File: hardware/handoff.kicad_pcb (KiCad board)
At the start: 2 copper layers, 40 x 62 mm, 52 parts, among them J1 BAT XH-2, J2 PAD JST-XH 2p, J3 LED JST-XH 4p / 5mm RGB, J5 CHG XH-2, SW1 SS-12F23G5, SW2 TACT 6x6, U1 Raspberry Pi Pico 2 W, U2 MCP6292-E/MS

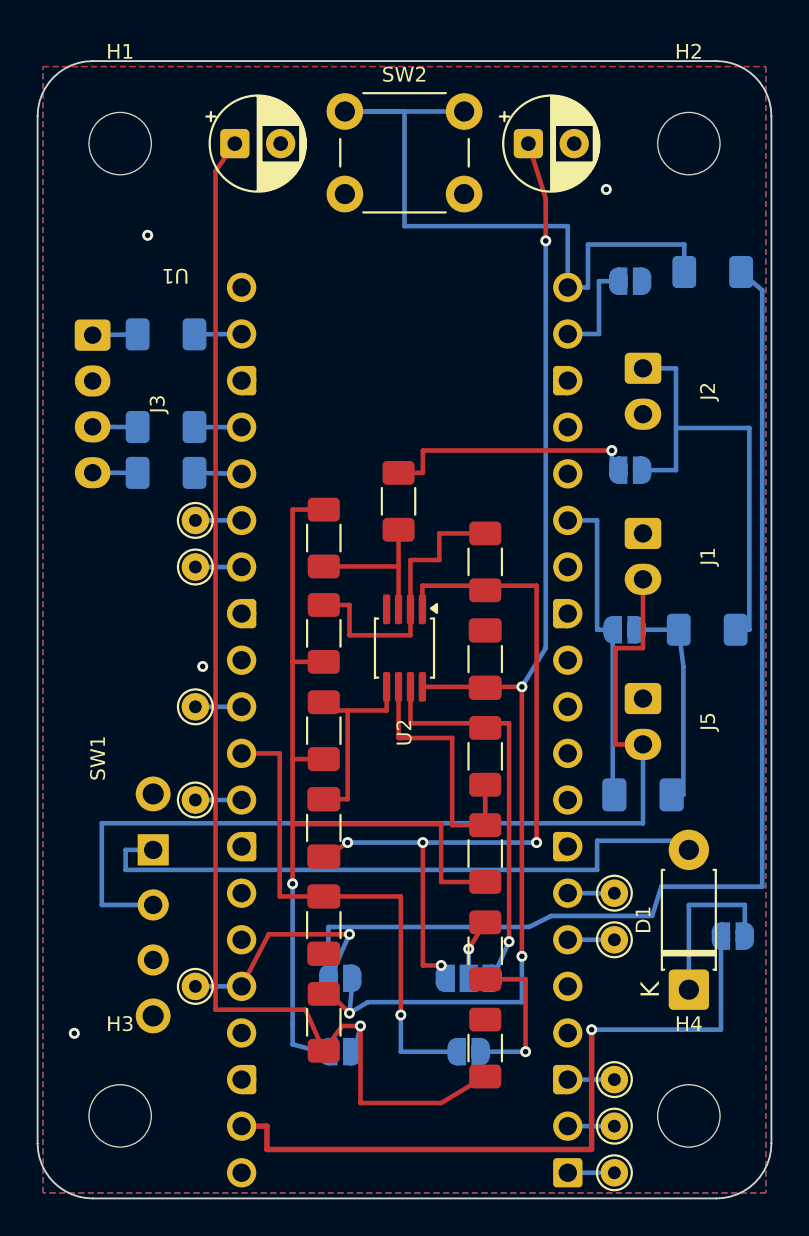
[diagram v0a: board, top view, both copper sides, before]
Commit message: Fix J3's overhang, the battery path, right-angle corners, edge clearance
Four things from the layout brief's known-wrong list, fixed together
because the battery path fix moved everything else on the thumb and
little-finger walls:

- J3 no longer overhangs the thumb edge (pin 1 moved from x 3.0 to
  x 4.0, flush with the housing's own courtyard).
- BAT+, SW_OUT, D1_K and VSYS moved from the little-finger wall to the
  thumb wall, where SW1 and J3 already are: one crossing of the board
  instead of three, and two pin-row threads instead of six. The
  SW_OUT U-turn and the JP4 redundant loop went with the routing they
  were part of.
- Every track corner is 45 degrees or straight. mitre() chamfers every
  right-angle join in a ROUTES polyline before it becomes copper, and
  two DRC rules (track_angle, track_segment_length) fail the run if a
  right angle or a stub comes back.
- +3V3 came off the little-finger wall (0.375 mm from the edge at
  0.25 mm, less once Power tracks are actually 0.5 mm): it now
  crosses the board once, at the elbow, into R15.

The VREF divider (R10, R11, JP6) moved to the hand end with its own
hold-up cap C4, off the elbow block, which frees the top lane on the
thumb side that VSYS now needs and removes a via.

Every footprint and text is now checked against the outline
programmatically (report()), not by eye: nothing may sit within
0.5 mm of the edge unless it is in OVERHANG (SW1's handle, U1's USB
courtyard). An independent short check (shorts(), SHAPE.Collide over
every pad/track/via/pour pair on each face) finds nothing under
0.2 mm. Board corners are fixed to 90-degree arcs (SetArcGeometry
with the midpoint on the corner; SetCenter/Start/End had been going
the long way round).

DRC: 0 error(s), 10 warning(s) (the ten deliberate
lib_footprint_mismatch); parity 0; unrouted 0 item(s).

Co-Authored-By: Claude Sonnet 5 <noreply@anthropic.com>
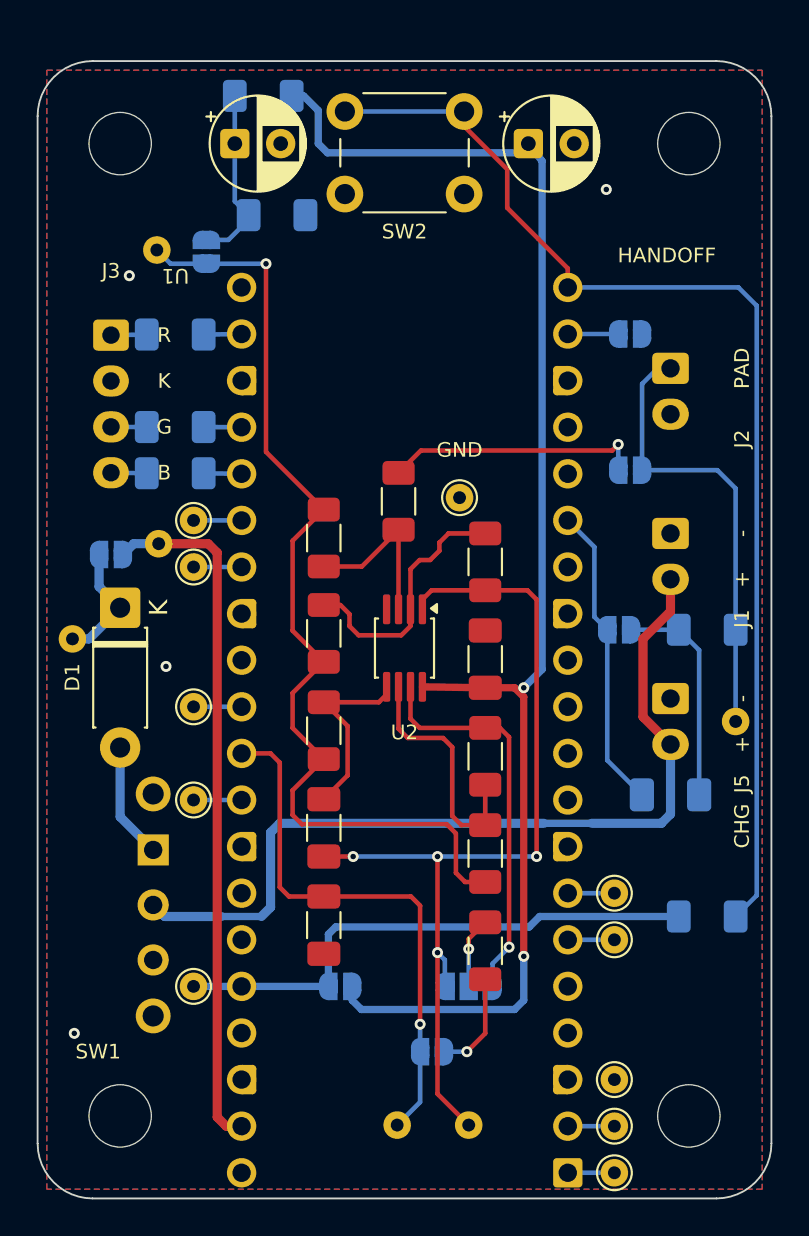
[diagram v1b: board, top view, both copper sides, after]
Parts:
- added TP1: GND, TestPoint:TestPoint_THTPad_D1.5mm_Drill0.7mm, F.Cu at (23.0, 23.8)
- added TP2: ADC0, TestPoint:TestPoint_THTPad_D1.5mm_Drill0.7mm, B.Cu at (19.6, 58.0)
- added TP3: OUT1, TestPoint:TestPoint_THTPad_D1.5mm_Drill0.7mm, B.Cu at (23.5, 58.0)
- added TP4: VREF, TestPoint:TestPoint_THTPad_D1.5mm_Drill0.7mm, B.Cu at (6.50, 10.3)
- added TP5: PAD, TestPoint:TestPoint_THTPad_D1.5mm_Drill0.7mm, B.Cu at (38.0, 36.0)
- added TP6: VSYS, TestPoint:TestPoint_THTPad_D1.5mm_Drill0.7mm, B.Cu at (6.60, 26.3)
- added TP7: D1_K, TestPoint:TestPoint_THTPad_D1.5mm_Drill0.7mm, B.Cu at (1.90, 31.5)
- R10, R11: moved to B.Cu
- moved R10 50.6 mm to (12.3, 1.90), turned to 180 degrees
- moved R11 46.8 mm to (13.1, 8.40), turned to 0 degrees
- moved JP6 44.2 mm to (9.20, 10.4), turned to -90 degrees
- moved JP5 39.8 mm to (4.00, 26.9), turned to 0 degrees
- moved D1 37.3 mm to (4.50, 29.8), turned to -90 degrees
- moved R15 35.1 mm to (36.5, 46.6), turned to 0 degrees
- moved JP8 2.88 mm to (32.3, 14.9)
- moved JP1 2.00 mm to (21.5, 54.0)
- moved C6 1.50 mm to (34.5, 40.0)
- moved J1 1.50 mm to (34.5, 25.8)
- moved J2 1.50 mm to (34.5, 16.8)
- moved J5 1.50 mm to (34.5, 34.8)
- moved J3 1.00 mm to (4.00, 14.9)
- moved R14 0.50 mm to (7.50, 22.5)
- moved R12 0.50 mm to (7.50, 14.9)
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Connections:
- net Net-(D1-K) renamed /D1_K
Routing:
- net Net-(JP6-A): track 69.9 -> 9.82 mm, vias 1 -> 0
- net +3V3: track 74.0 -> 29.7 mm, vias 1 -> 0
- net /SW_OUT: track 35.4 -> 6.33 mm
- net /BTN: track 38.4 -> 62.9 mm
- net /AFE_3V3: track 65.3 -> 78.6 mm, vias 4 -> 2
- net /OUT1: track 41.3 -> 50.1 mm
- net /BAT+: track 53.0 -> 47.2 mm
- net VREF: track 49.5 -> 54.4 mm
- net Net-(JP1-A): track 8.60 -> 5.61 mm
- net /ROLE: track 5.63 -> 2.75 mm
- net /ADC0: track 27.1 -> 29.6 mm
- net /D1_K: track 9.07 -> 6.68 mm
- net GND: track 2.30 -> 0.00 mm
- net Net-(U2A--): track 16.0 -> 14.2 mm
- net VSYS: track 39.0 -> 37.9 mm, vias 1 -> 0
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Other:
- board text added: "+"
- board text added: "-"
- board text added: "ADC0"
- board text added: "B"
- board text added: "CHG"
- board text added: "D1K"
- board text added: "G"
- board text added: "GND"
- board text added: "HANDOFF"
- board text added: "HANDOFF rev A - 2 layer, 40 x 62 mm, 1.6 mm FR-4, 1 oz Cu, HASL lead-free, green mask, white silk. Min track/space 0.25/0.2 (design), 0.15 (fab floor). Min drill 0.3 (vias), 0.7 (test pads). H1-H4 3.4 mm unplated."
- board text added: "HANDOFF rev A 2026-09"
- board text added: "JP1-8: OPEN = ISOLATED"
- board text added: "K"
- board text added: "OUT1"
- board text added: "PAD"
- board text added: "R"
- board text added: "VREF"
- board text added: "VSYS"

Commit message: Add the haptic motor, move the passives to 0603/0805, unstick the breakout pads
Three changes to the parts order, and one bug they surfaced.

The motor. A 10 mm coin motor (M1, off-board on leads into J6) switched
low-side by an AO3400A (Q1) from GP28, with a 100 R gate series (R16), a
100 k gate pull-down (R17, so the gate cannot float through BOOTSEL) and a
SOD-123 Schottky (D3) across the motor. It runs from VSYS, not the Pico's
3V3: 100 mA of pulsed motor current has no business on the rail that feeds
AFE_3V3 through JP4. The block sits on the bottom face at the thumb end of
the elbow, two millimetres from VSYS at pin 39 and a pour away from the AFE.
D3 has no SKU yet - it is the one part here not already on order.

The passives. 100 k, 10 k and the LED series resistors (now 100 R, not
330 R) are 0603; C4 and C5 are 0805 MLCC instead of 5 mm radial
electrolytics. 1 M, 1k5 and the C0G/X7R capacitors stay 1206 - they were not
re-ordered. Every 0603 pad moved 0.64 mm inward, which walked twenty-odd
track ends off their pads, so ROUTES now names pads - P("R6", "1") - and
gen_pcb.py resolves them against the placed footprint. The shift also closed
the 0.25 mm pour channel under R5 that is the AFE pour's only way out to the
electrode; R5 moved back 0.64 mm and VREF leaves its pad along the pad row
now. C4 and C5 changed face: their feeds were always on the bottom and
reached them through the electrolytics' leads.

The bug. E3, E4 and E10 broke out Pico pins 1, 2 and 3 at x 31.44, which put
their pads 3.3 mm from H4's centre - inside the 8 mm enclosure boss. DRC
missed it because the boss keep-out allows pads (the hole's own NPTH pad is
in the middle of it) and because the "bare pads have no body" rule excused
the courtyard overlap from either side. Both are fixed: report() checks every
pad against every boss circle, and the courtyard exemption no longer applies
against a mounting hole. Regression-tested. The breakouts are now GP3 (5),
GP22 (29) and GND (8); GP0 and GP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
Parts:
- added D3: 1N5819W, Diode_SMD:D_SOD-123, F.Cu at (16.9, 58.6)
- added J6: MOT 1x02 2.54, Connector_PinHeader_2.54mm:PinHeader_1x02_P2.54mm_Vertical, B.Cu at (14.9, 53.7)
- added Q1: AO3400A, Package_TO_SOT_SMD:SOT-23, B.Cu at (15.0, 60.0)
- added R16: 100, Resistor_SMD:R_0603_1608Metric_Pad0.98x0.95mm_HandSolder, F.Cu at (13.6, 47.9)
- added R17: 100k, Resistor_SMD:R_0603_1608Metric_Pad0.98x0.95mm_HandSolder, F.Cu at (14.5, 51.3)
- added TP8: AFE_3V3, TestPoint:TestPoint_THTPad_D1.5mm_Drill0.7mm, B.Cu at (27.5, 8.20)
- C4, C5: value 10uF 63V -> 10uF 100V; footprint Capacitor_THT:CP_Radial_D5.0mm_P2.50mm -> Capacitor_SMD:C_0805_2012Metric_Pad1.18x1.45mm_HandSolder; moved to B.Cu
- E10: value GND (pin 3) -> GND (pin 8)
- E3: value GP0 (pin 1) -> GP3 (pin 5)
- E4: value GP1 (pin 2) -> GP22 (pin 29)
- R10, R11, R15, R4, R5, R6, R7, R8: footprint Resistor_SMD:R_1206_3216Metric_Pad1.30x1.75mm_HandSolder -> Resistor_SMD:R_0603_1608Metric_Pad0.98x0.95mm_HandSolder
- R12, R13, R14: value 330 -> 100; footprint Resistor_SMD:R_1206_3216Metric_Pad1.30x1.75mm_HandSolder -> Resistor_SMD:R_0603_1608Metric_Pad0.98x0.95mm_HandSolder
- moved E4 34.2 mm to (8.50, 32.7)
- moved E10 12.7 mm to (31.4, 42.8)
- moved E3 10.2 mm to (31.4, 50.4)
- moved C4 1.25 mm to (11.8, 5.20)
- moved C5 1.04 mm to (27.8, 4.50)
- moved R10 0.64 mm to (11.7, 1.90)
- moved R11 0.64 mm to (12.4, 8.40)
- moved R5 0.64 mm to (15.6, 30.6)
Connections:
- E3 pad 1: /GP0 -> /GP3
- E4 pad 1: /GP1 -> /GP22
- U1 pad 1: /GP0 -> unconnected-(U1-GPIO0-Pad1)
- U1 pad 2: /GP1 -> unconnected-(U1-GPIO1-Pad2)
- U1 pad 29: unconnected-(U1-GPIO22-Pad29) -> /GP22
- U1 pad 34: unconnected-(U1-GPIO28_ADC2-Pad34) -> /MOT_DRV
- U1 pad 5: unconnected-(U1-GPIO3-Pad5) -> /GP3
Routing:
- net Net-(Q1-G): track 0.00 -> 13.5 mm, vias 0 -> 1
- net /MOT_SW: track 0.00 -> 10.2 mm, vias 0 -> 1
- net VSYS: track 37.9 -> 44.8 mm
- net /MOT_DRV: track 0.00 -> 3.37 mm
- net /GP22: track 0.00 -> 2.62 mm
- net /GP3: track 0.00 -> 2.30 mm
- net /GP1: track 2.30 -> 0.00 mm
- net /GP0: track 2.30 -> 0.00 mm
- net GND: track 0.00 -> 2.12 mm, vias 4 -> 5
- net Net-(U2B--): track 13.6 -> 12.0 mm
- net /AFE_3V3: track 78.6 -> 79.9 mm
- net /OUT1: track 50.1 -> 51.4 mm
- net +3V3: track 29.7 -> 30.3 mm
- net /LED_G: track 2.07 -> 2.71 mm
- net /J3_G: track 1.95 -> 2.59 mm
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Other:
- board text added: "HANDOFF rev A - 2 layer, 40 x 62 mm, 1.6 mm FR-4, 1 oz Cu, HASL lead-free, green mask, white silk. Min track/space 0.25/0.2 (design), 0.15 (fab floor). Min solder-mask dam 0.1. Drills 0.3 / 0.7 / 0.95 / 1.0 / 1.1 / 1.15 PTH and 3.4 NPTH - see build/drills.md. H1-H4 3.4 mm unplated, each inside an 8 mm enclosure boss."
- board text added: "JP1-8 = OPEN"
- board text added: "MOT"
- board text removed: "HANDOFF rev A - 2 layer, 40 x 62 mm, 1.6 mm FR-4, 1 oz Cu, HASL lead-free, green mask, white silk. Min track/space 0.25/0.2 (design), 0.15 (fab floor). Min drill 0.3 (vias), 0.7 (test pads). H1-H4 3.4 mm unplated."
- board text removed: "JP1-8: OPEN = ISOLATED"

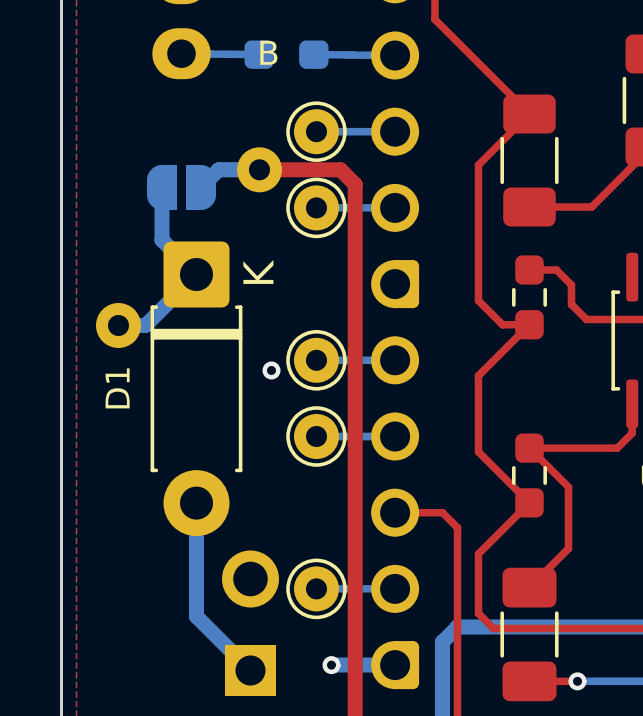
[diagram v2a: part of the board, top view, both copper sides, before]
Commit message: Move D1 to the SS220F Schottky (SMB); D3 stays SOD-123
D1 and D3 were both candidates for a single SS220F (Slkor, 200 V 2 A,
SMB/DO-214AA) SKU to replace their 1N5819 parts. D1 took the swap: its
THT DO-41 pads used to be copper on both faces, so its approach tracks
just ended on the pad; SMD is F.Cu only, so each track's existing 45
degree bend became a via with a short F.Cu stub into the pad, and the
oversized SMB body outline moved off silk to stop it clipping TP7.

D3 does not fit: the motor block is a 6 x 9 mm pocket already holding
J6, Q1, R16 and R17, and SMB's courtyard swallowed J6's pad, hung off
the board edge, and clipped two neighbours' solder mask. Left as
1N5819W/SOD-123 pending a decision on a smaller-package Schottky or a
new location for it.

Co-Authored-By: Claude Sonnet 5 <noreply@anthropic.com>
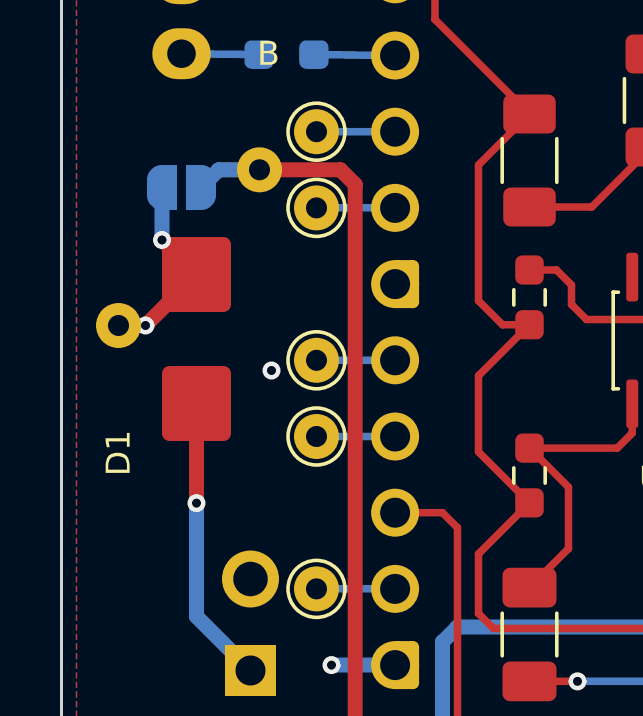
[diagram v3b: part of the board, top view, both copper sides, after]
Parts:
- D1: value 1N5819 -> SS220F; footprint Diode_THT:D_DO-41_SOD81_P7.62mm_Horizontal -> Diode_SMD:D_SMB
- moved D1 2.15 mm to (4.50, 31.9)
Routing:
- net /SW_OUT: track 6.33 -> 9.65 mm, vias 0 -> 1
- net /D1_K: vias 0 -> 2
